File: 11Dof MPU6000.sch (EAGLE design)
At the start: 20 parts, among them J401 M12PTH, U101 BMP180, U401 SN74LVC1G32, U501 L3G4200D, U601 BMA180, U801 5883

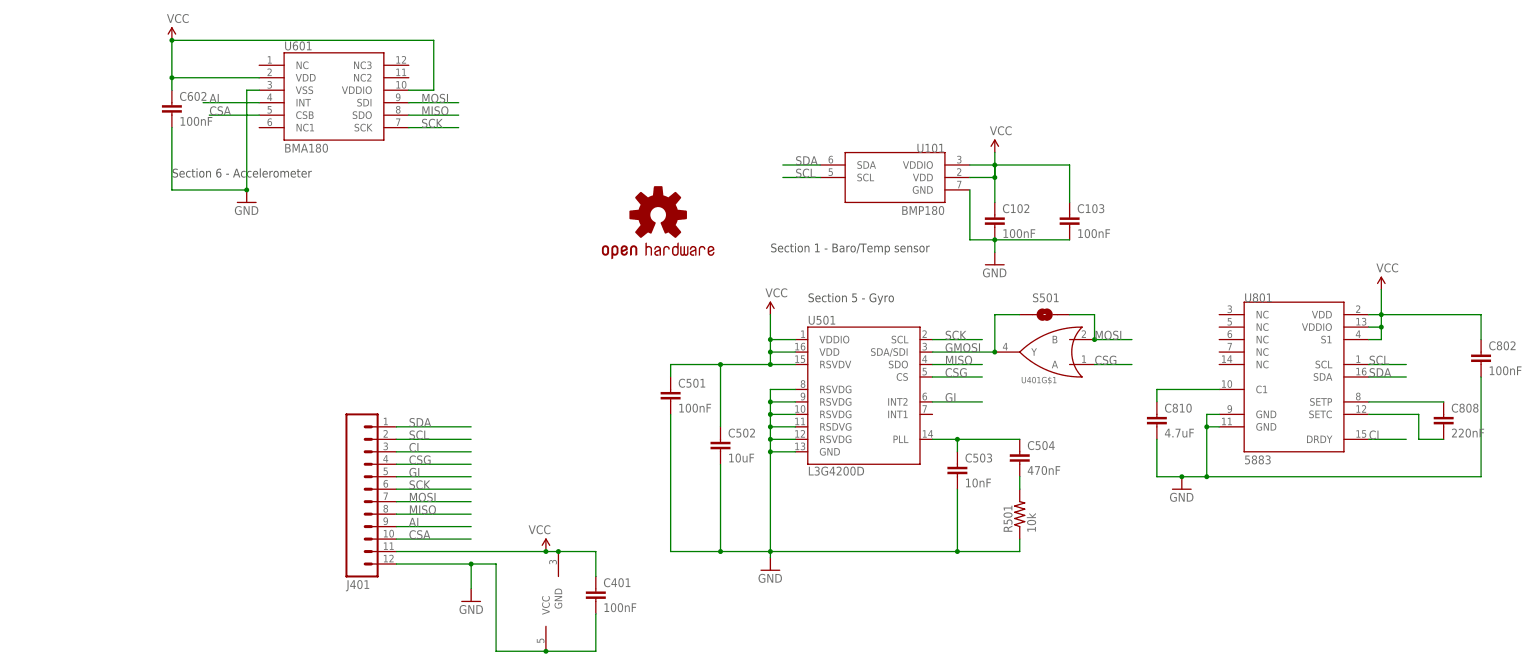
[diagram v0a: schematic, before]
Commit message: Made 11DoF for BMA180, MPU6000, replaced ADXL345 with BMA180 in Rocketometer2148, made Rocketometer2148 with MPU6000
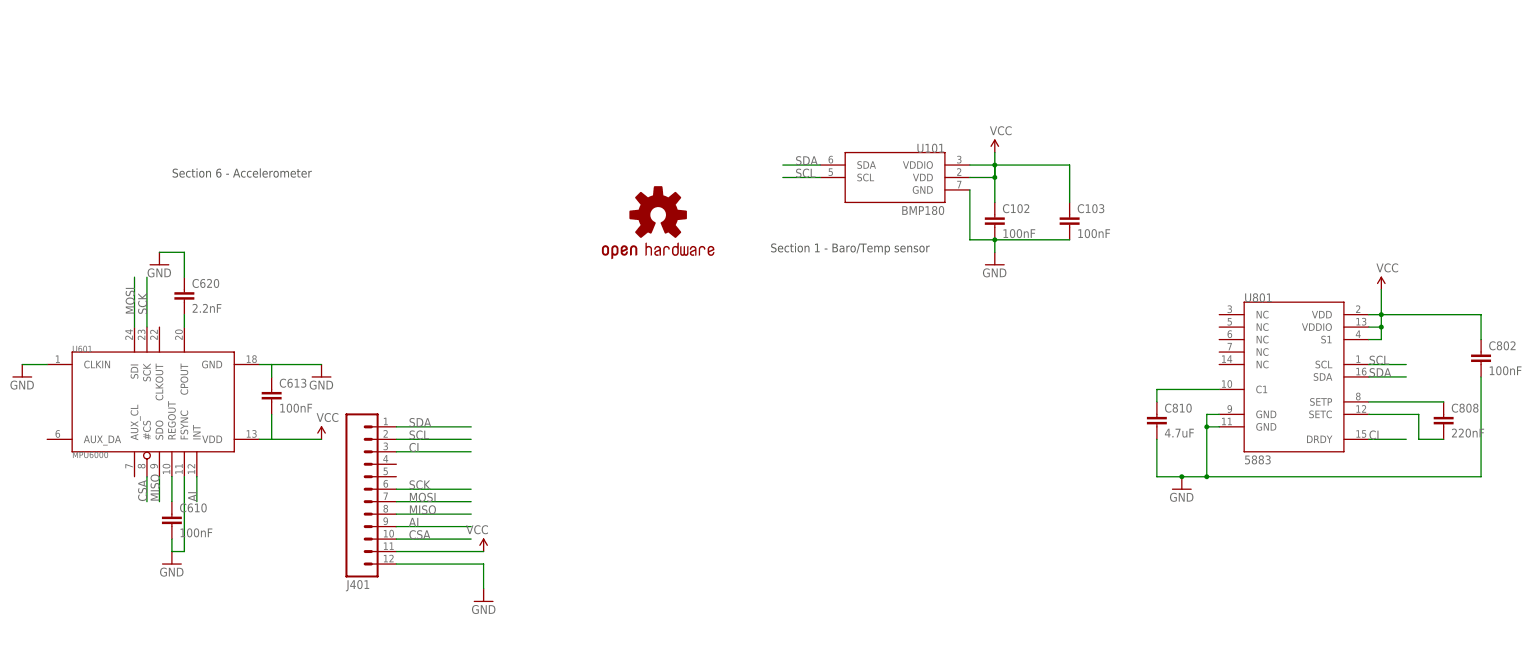
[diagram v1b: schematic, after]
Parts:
- removed C401, C501, C602: 100nF, SparkFun:CAP0603-CAP
- removed C502: 10uF, SparkFun:CAP0603-CAP
- removed C503: 10nF, SparkFun:CAP0603-CAP
- removed C504: 470nF, SparkFun:CAP0603-CAP
- removed R501: 10k, SparkFun:RESISTOR0603-RES
- removed S501: SOLDERJUMPERNO, SparkFun:SOLDERJUMPERNO
- removed U401: SN74LVC1G32, KwanSystems:SN74LVC1G32
- removed U501: L3G4200D, SparkFun:L3G4200D
- added C610, C613: 100nF, SparkFun:CAP0603-CAP
- added C620: 2.2nF, SparkFun:CAP0603-CAP
- U601: value BMA180 -> MPU6000; device SparkFun-Sensors:BMA180 -> KwanSystems:MPU6000
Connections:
- removed net CSG: J401.4, U401G$1.A, U501.CS
- removed net GI: J401.5, U501.INT2
- removed net GMOSI: S501.1, U401G$1.Y, U501.SDA/SDI
- removed net N$2: C504.2, R501.2
- new net N$3: C620.2, U601.CPOUT
- net CSA: now also U601.#CS; no longer U601.CSB
- net GND: now also C610.2, C613.1, C620.1, U601.CLKIN, U601.FSYNC, U601.GND; no longer C401.2, C501.2, C502.2, C503.2, C602.2, R501.1, U401G$2.VCC, U501.GND, U501.RSDVG@3, U501.RSVDG@0, U501.RSVDG@1, U501.RSVDG@2, U501.RSVDG@4, U601.VSS
- net MISO: no longer U501.SDO
- net MOSI: no longer S501.2, U401G$1.B
- net N$1: now also C610.1, U601.REGOUT; no longer C503.1, C504.1, U501.PLL
- net SCK: no longer U501.SCL
- net VCC: now also C613.2; no longer C401.1, C501.1, C502.1, C602.1, U401G$2.GND, U501.RSVDV@0, U501.VDD, U501.VDDIO, U601.VDDIO
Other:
- note removed: "Section 5 - Gyro"
